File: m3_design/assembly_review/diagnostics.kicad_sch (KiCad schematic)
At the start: 12 parts, among them U6 SAM-M10Q-00B

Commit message: Make R2 orderable: stocked drop-ins, JLC placement corrections, ordering guide
- Stock (JLC assembly API): U8 AP63200 -> AP63300WU-7 (same TSOT26 pinout,
  VFB, fsw), L3 -> SRP5030T-6R8M (same body/land, AP63300 Table 1), C77
  100p -> 47p (Table 1), C84 25SVPF330M -> 35SVPK330M (same OS-CON F12).
  Every BOM line now has JLC stock for 5 boards except U6 SAM-M10Q
  (consign / Global Sourcing; DigiKey has stock).
- tools/jlc_orient.py matches each footprint pad-by-pad to the LCSC/EasyEDA
  footprint of its LCSC code; export_fab.py applies the rotation/offset.
  Without it U7, U8, U10, U11, U12, U13, D121 and LED2 would be rotated.
- tools/jlc_stock.py: repeatable stock check; fab/stock_check.json.
- JLC_Assembly field: U6 consign note, J2/J123 hand-cut from one 1x40 strip.
- docs/ORDERING.md: PCB options, PCBA, preview checklist, off-board parts.

DRC 0 / unconnected 0 / parity 0 / ERC 0, audit OK; contract OK;
tests 173/112/12 pass; sim 135 PASS.

Co-Authored-By: Claude Opus 5.5 (1M context) <noreply@anthropic.com>
Claude-Session: https://claude.ai/code/session_01DdkfTxR7SVyv9xZNmPk9vB
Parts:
- U6: JLC_Assembly (none) -> Consign or JLC Global Sourcing: SAM-M10Q-00B from DigiKey (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
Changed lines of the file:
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@@
+				(font
+					(size 1.27 1.27))))
+		(property "JLC_Assembly" "Consign or JLC Global Sourcing: SAM-M10Q-00B from DigiKey (JLC stock 0 on 2026-09-27)"
+			(at 91.44 83.82 0)
+			(hide yes)
+			(effects
 				(font
 					(size 1.27 1.27))))

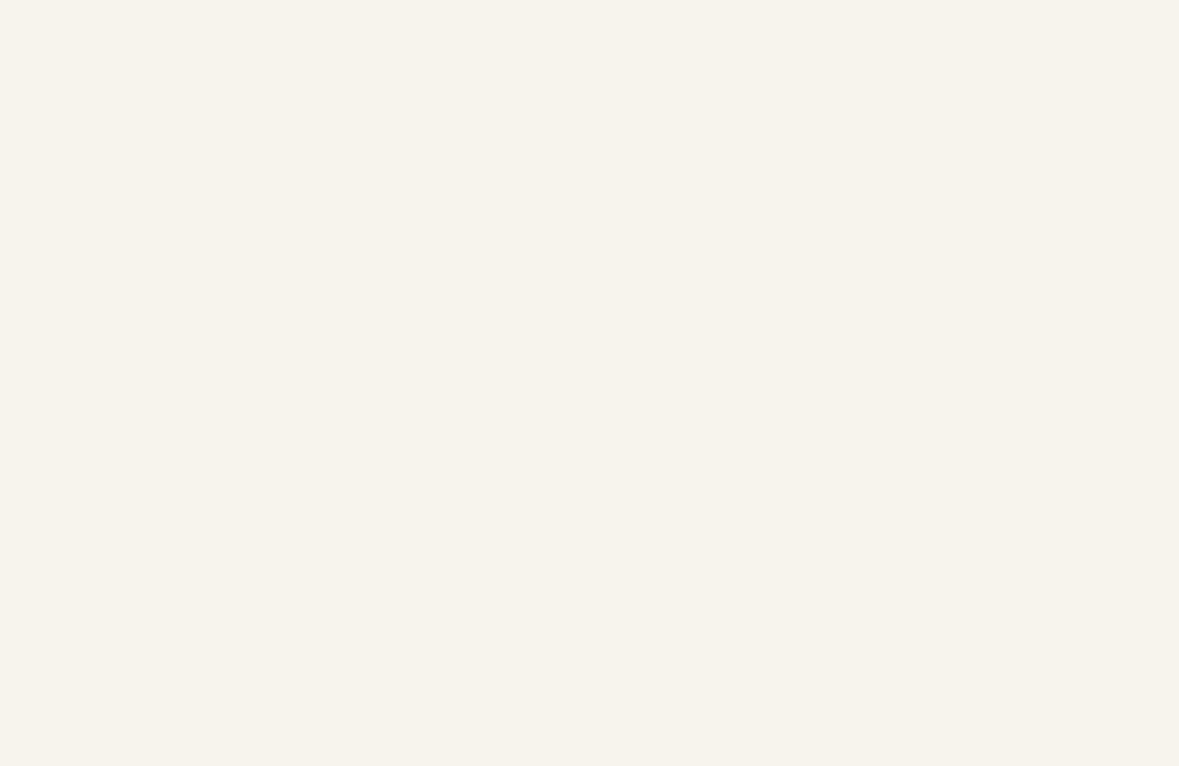
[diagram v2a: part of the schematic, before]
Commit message: Add CAM_5V sense (R104/R105/C94 -> PB1) so the USB self-test covers the camera regulator
AUTOTEST_DESIGN's sensing set is already on R2 (VLOGIC, 3V3, RAW_ACT, VBUS,
arm/continuity with cold pull-up, internal channels, buzzer load step); the
new camera branch had only a fault flag. CAM_5V x 1k/11k -> PB1 (ADC12_INP5):
0.477 V at 5.25 V, 1.40 V at the 15.4 V TVS clamp (< TT 4.0 V). Live only
while the board and the camera branch are powered, so no always-live path
into an unpowered MCU (AUTOTEST 2.4). Parts reuse existing LCSC codes.

Routed out from U1's outer side (0/45/90, 4 vias), no fan-out inside the
LQFP ring. DRC 0 / unconnected 0 / parity 0 / ERC 0, audit OK; tests pass;
CPL fully orientation-corrected; stock OK for 5 boards except U6.

Co-Authored-By: Claude Opus 5.5 (1M context) <noreply@anthropic.com>
Claude-Session: https://claude.ai/code/session_01DdkfTxR7SVyv9xZNmPk9vB
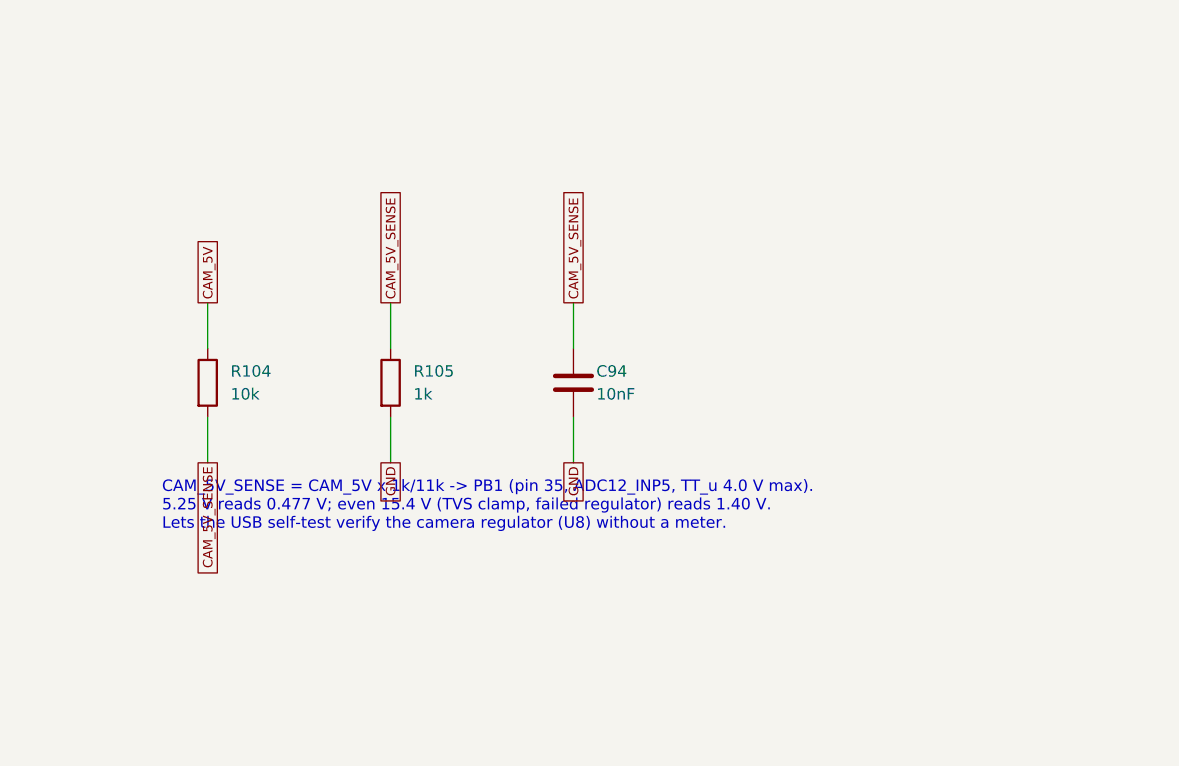
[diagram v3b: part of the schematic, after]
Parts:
- added C94: 10nF, rocket:C0603, symbol M3:C
- added R104: 10k, rocket:R0402, symbol M3:R
- added R105: 1k, rocket:R0402, symbol M3:R
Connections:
- net GND: now also C94.2, R105.2
- new net CAM_5V: R104.1
- new net CAM_5V_SENSE: C94.1, R104.2, R105.1
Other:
- note added: "CAM_5V_SENSE = CAM_5V x 1k/11k -> PB1 (pin 35, ADC12_INP5, TT_u 4.0 V max). 5.25 V reads 0.477 V; even 15.4 V (TVS clamp, failed regulator) reads 1.40 V. Lets the USB self-test verify the camera regulator (U8) without a meter."
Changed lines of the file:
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@@
 			(justify left))
+)
+	(symbol
+		(lib_id "M3:R")
+		(at 101.60 200.66 0)
+		(unit 1)
+		(in_bom yes)
+		(on_board yes)
+		(dnp no)
+		(property "Reference" "R104"
+			(at 104.14 199.39 0)
+			(effects
+				(font
+					(size 1.27 1.27))
+				(justify left)))
+		(property "Value" "10k"
+			(at 104.14 201.93 0)
+			(effects
+				(font
+					(size 1.27 1.27))
+				(justify left)))
+		(property "Footprint" "rocket:R0402"
+			(at 101.60 200.66 0)
+			(hide yes)
+			(effects
+				(font
+					(size 1.27 1.27))
+				(justify left)))
+		(property "Datasheet" ""
+			(at 101.60 200.66 0)
+			(hide yes)
+			(effects
+				(font
+					(size 1.27 1.27))
+				(justify left)))
+		(property "LCSC" "C25744"
+			(at 101.60 200.66 0)
+			(hide yes)
+			(effects
+				(font
+					(size 1.27 1.27))
+				(justify left)))
+		(instances
+			(project "m3"
+				(path "/6007a7db-6a58-5660-8beb-956dea045ff8/0e505cf1-213a-5be0-ba23-0f8cc47b8f19"
+					(reference "R104")
+					(unit 1)))))
+	(wire
+		(pts
+			(xy 101.6 196.85)
+			(xy 101.6 191.77))
+		(stroke
+			(width 0)
+			(type default))
+)
+	(global_label "CAM_5V"
+		(shape passive)
+		(at 101.6 191.77 90)
+		(effects
+			(font
+				(size 1.05 1.05))
+			(justify left))
+)
+	(wire
+		(pts
+			(xy 101.6 204.47)
+			(xy 101.6 209.55))
+		(stroke
+			(width 0)
+			(type default))
+)
+	(global_label "CAM_5V_SENSE"
+		(shape passive)
+		(at 101.6 209.55 270)
+		(effects
+			(font
+				(size 1.05 1.05))
+			(justify right))
+)
+	(symbol
+		(lib_id "M3:R")
+		(at 121.92 200.66 0)
+		(unit 1)
+		(in_bom yes)
+		(on_board yes)
+		(dnp no)
+		(property "Reference" "R105"
+			(at 124.46 199.39 0)
+			(effects
+				(font
+					(size 1.27 1.27))
+				(justify left)))
+		(property "Value" "1k"
+			(at 124.46 201.93 0)
+			(effects
+				(font
+					(size 1.27 1.27))
+				(justify left)))
+		(property "Footprint" "rocket:R0402"
+			(at 121.92 200.66 0)
+			(hide yes)
+			(effects
+				(font
+					(size 1.27 1.27))
+				(justify left)))
+		(property "Datasheet" ""
+			(at 121.92 200.66 0)
+			(hide yes)
+			(effects
+				(font
+					(size 1.27 1.27))
+				(justify left)))
+		(property "LCSC" "C11702"
+			(at 121.92 200.66 0)
+			(hide yes)
+			(effects
+				(font
+					(size 1.27 1.27))
+				(justify left)))
+		(instances
+			(project "m3"
+				(path "/6007a7db-6a58-5660-8beb-956dea045ff8/0e505cf1-213a-5be0-ba23-0f8cc47b8f19"
+					(reference "R105")
+					(unit 1)))))
+	(wire
+		(pts
+			(xy 121.92 196.85)
+			(xy 121.92 191.77))
+		(stroke
+			(width 0)
+			(type default))
+)
+	(global_label "CAM_5V_SENSE"
+		(shape passive)
+		(at 121.92 191.77 90)
+		(effects
+			(font
+				(size 1.05 1.05))
+			(justify left))
+)
+	(wire
+		(pts
+			(xy 121.92 204.47)
+			(xy 121.92 209.55))
+		(stroke
+			(width 0)
+			(type default))
+)
+	(global_label "GND"
+		(shape passive)
+		(at 121.92 209.55 270)
+		(effects
+			(font
+				(size 1.05 1.05))
+			(justify right))
+)
+	(symbol
+		(lib_id "M3:C")
+		(at 142.24 200.66 0)
+		(unit 1)
+		(in_bom yes)
+		(on_board yes)
+		(dnp no)
+		(property "Reference" "C94"
+			(at 144.78 199.39 0)
+			(effects
+				(font
+					(size 1.27 1.27))
+				(justify left)))
+		(property "Value" "10nF"
+			(at 144.78 201.93 0)
+			(effects
+				(font
+					(size 1.27 1.27))
+				(justify left)))
+		(property "Footprint" "rocket:C0603"
+			(at 142.24 200.66 0)
+			(hide yes)
+			(effects
+				(font
+					(size 1.27 1.27))
+				(justify left)))
+		(property "Datasheet" ""
+			(at 142.24 200.66 0)
+			(hide yes)
+			(effects
+				(font
+					(size 1.27 1.27))
+				(justify left)))
+		(property "LCSC" "C57112"
+			(at 142.24 200.66 0)
+			(hide yes)
+			(effects
+				(font
+					(size 1.27 1.27))
+				(justify left)))
+		(instances
+			(project "m3"
+				(path "/6007a7db-6a58-5660-8beb-956dea045ff8/0e505cf1-213a-5be0-ba23-0f8cc47b8f19"
+					(reference "C94")
+					(unit 1)))))
+	(wire
+		(pts
+			(xy 142.24 196.85)
+			(xy 142.24 191.77))
+		(stroke
+			(width 0)
+			(type default))
+)
+	(global_label "CAM_5V_SENSE"
+		(shape passive)
+		(at 142.24 191.77 90)
+		(effects
+			(font
+				(size 1.05 1.05))
+			(justify left))
+)
+	(wire
+		(pts
+			(xy 142.24 204.47)
+			(xy 142.24 209.55))
+		(stroke
+			(width 0)
+			(type default))
+)
+	(global_label "GND"
+		(shape passive)
+		(at 142.24 209.55 270)
+		(effects
+			(font
+				(size 1.05 1.05))
+			(justify right))
+)
+	(text "CAM_5V_SENSE = CAM_5V x 1k/11k -> PB1 (pin 35, ADC12_INP5, TT_u 4.0 V max).\n5.25 V reads 0.477 V; even 15.4 V (TVS clamp, failed regulator) reads 1.40 V.\nLets the USB self-test verify the camera regulator (U8) without a meter."
+		(exclude_from_sim no)
+		(at 96.52 217.17 0)
+		(effects
+			(font
+				(size 1.27 1.27))
+			(justify left bottom))
 )
 	(sheet_instances

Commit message: M3-ASSY-R3: remove GNSS, cut board to 46 x 193 mm
Schematic: U6/C33/C34 and GPS_TX/GPS_RX removed, PC6/PC7 no-connect, sheet 04
renamed, title-block revision R3 on all 14 sheets. PCB: m3_design/r3_cut.py deletes
227 tracks/vias (GPS nets, the U6-only 3V3A branch, forward GND stitching) and
U6/C33/C34; outline 46 x 193 mm, forward M3 pair moved to y = 189, GND zones
trimmed and refilled. No remaining track, via or footprint moved (checked
against R2). check.sh: DRC 0, unconnected 0, parity 0, ERC 0, audit OK;
check_actuators OK. Sheets, netlist, DRC/ERC evidence and renders regenerated.

Co-Authored-By: Claude Opus 5.5 <noreply@anthropic.com>
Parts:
- removed C33: 100nF, rocket:C0402, symbol M3:C
- removed C34: 22uF, rocket:C0805, symbol M3:C
- removed U6: SAM-M10Q-00B, rocket:LCC-20_L15.5-W15.5-P1.90_SAM-M10Q-00B, symbol M3:GNSS
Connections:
- no-connect marks 7 -> 0
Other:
- note added: "04 | Voltage diagnosis and indicators"
- note removed: "04 | Voltage diagnosis, indicators and GNSS receiver"
- note removed: "U6 fitted: SAM-M10Q-00B. V_BCKP remains NC; no backup supply (UBX-22020019 R02 4.1.3)."
- title: 04 | Voltage diagnosis, indicators and GNSS receiver -> 04 | Voltage diagnosis and indicators

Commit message: M3-ASSY-R4: R3 validation fixes, new IMU, fault-tolerant pyro sensing
The board, schematic sheets and footprint library are generated from
R3 (533af8e) by m3_design/r4_build.sh (r4_lib.py, r4_sch.py,
r4_pcb.py). docs/REQUIREMENTS.md states what the board must do;
docs/M3_R4.md records every change, the thirteen evaluation passes
(twelve independent reviews) and the accepted deviations.

- IMU: ST LSM6DSV320X (16 g and 320 g, 4000 dps)
- Pyro: black ARM and orange igniter terminals, eight pyro spacing
  rules in m3.kicad_dru, sense dividers of 2 x 5.1k over 2 x 2k in
  parallel, 4.7k at each ADC pin (R168-R172)
- Pull-pin on a JST PH connector; JLC tooling holes
- Fab: Standard PCBA, 84 BOM lines, 205 placed parts, $80.12 per board
  at five boards (tools/jlc_cost.py); placement rotations verified
- Gate: tools/check.sh DRC 0, unconnected 0, schematic parity 0, ERC 0,
  audit OK; m3_design/check_actuators.py OK

Nothing has been built or measured, and there is no R4 firmware. The
open owner decisions and the bench tests are listed in STATUS.md.

Co-Authored-By: Claude Opus 5.5 <noreply@anthropic.com>
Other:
- note added: "CAM_5V_SENSE = CAM_5V x 1k/11k -> PB1 (pin 35, ADC12_INP5, TT_u 4.0 V max). 5.25 V reads 0.477 V; even 19.9 V (TVS clamp, failed regulator) reads 1.81 V. Lets the USB self-test verify the camera regulator (U8) without a meter."
- note removed: "CAM_5V_SENSE = CAM_5V x 1k/11k -> PB1 (pin 35, ADC12_INP5, TT_u 4.0 V max). 5.25 V reads 0.477 V; even 15.4 V (TVS clamp, failed regulator) reads 1.40 V. Lets the USB self-test verify the camera regulator (U8) without a meter."
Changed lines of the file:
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@@
 		(title "04 | Voltage diagnosis and indicators")
 		(date "2026-09-07")
-		(rev "M3-ASSY-R3")
+		(rev "M3-ASSY-R4")
 		(company "Single-board M3 candidate; full system incomplete"))
 	(text "04 | Voltage diagnosis and indicators"
@@
 			(justify right))
 )
-	(text "CAM_5V_SENSE = CAM_5V x 1k/11k -> PB1 (pin 35, ADC12_INP5, TT_u 4.0 V max).\n5.25 V reads 0.477 V; even 15.4 V (TVS clamp, failed regulator) reads 1.40 V.\nLets the USB self-test verify the camera regulator (U8) without a meter."
+	(text "CAM_5V_SENSE = CAM_5V x 1k/11k -> PB1 (pin 35, ADC12_INP5, TT_u 4.0 V max).\n5.25 V reads 0.477 V; even 19.9 V (TVS clamp, failed regulator) reads 1.81 V.\nLets the USB self-test verify the camera regulator (U8) without a meter."
 		(exclude_from_sim no)
 		(at 96.52 217.17 0)
